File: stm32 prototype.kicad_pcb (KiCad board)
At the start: 4 copper layers, 135 parts, among them J1 USB_B_Mini, J2 Conn_01x06, J3 Conn_01x02, J4 Conn_01x10, Q1 Q_NMOS_GSD, Q2 Q_NMOS_GSD, Q3 Q_NMOS_GSD, Q4 Q_NMOS_GSD, Q5 Q_NMOS_GSD, Q6 Q_NMOS_GSD, Q7 Q_NMOS_GSD, Q8 Q_NMOS_GSD, Q9 Q_NMOS_GSD, U1 FT232RL, U2 W25Q128JV-DTR, U3 STM32F407VGTx, U4 LD1117S33TR, U5 ESP32, U6 IS25LP016D-JNLE-TR, U7 TPS62203DBVR, Y1 Crystal_GND24, Y2 Crystal_GND24, Y3 Crystal_GND23

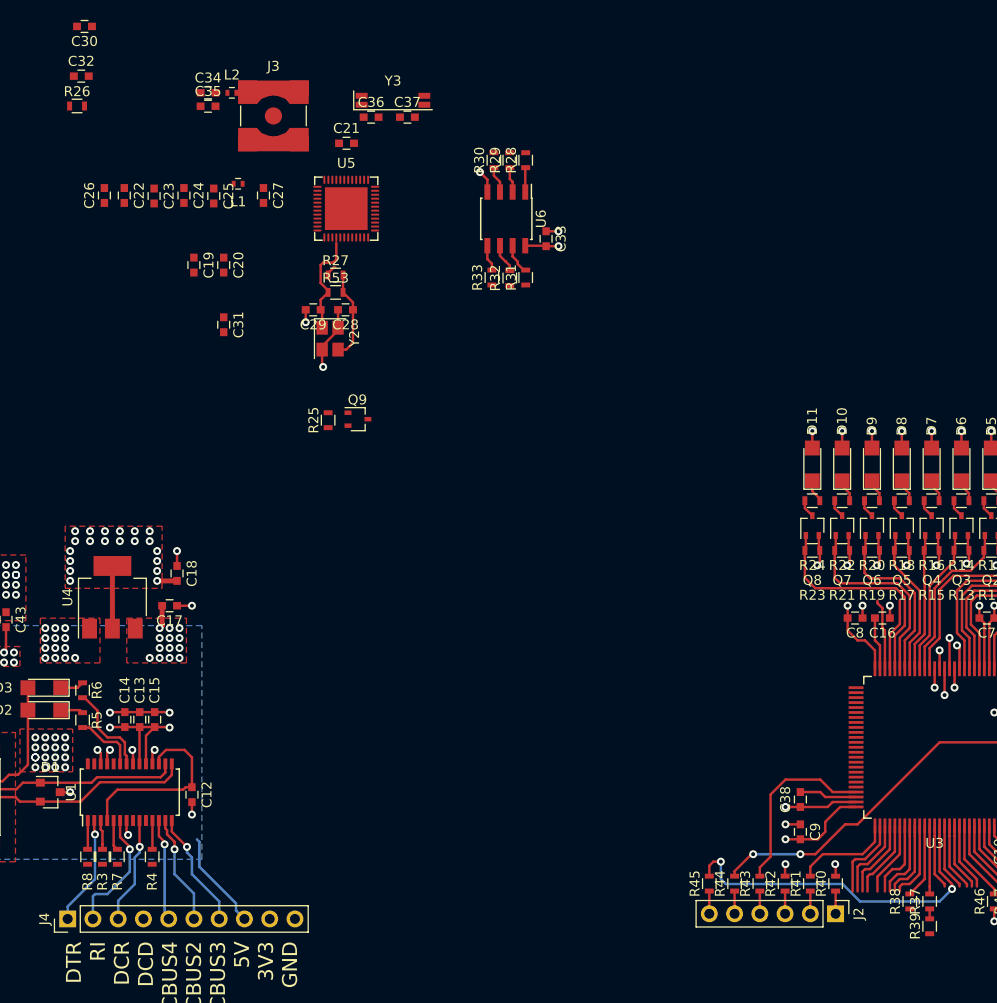
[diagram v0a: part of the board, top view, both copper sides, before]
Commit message: began switching to esp32-wroom module
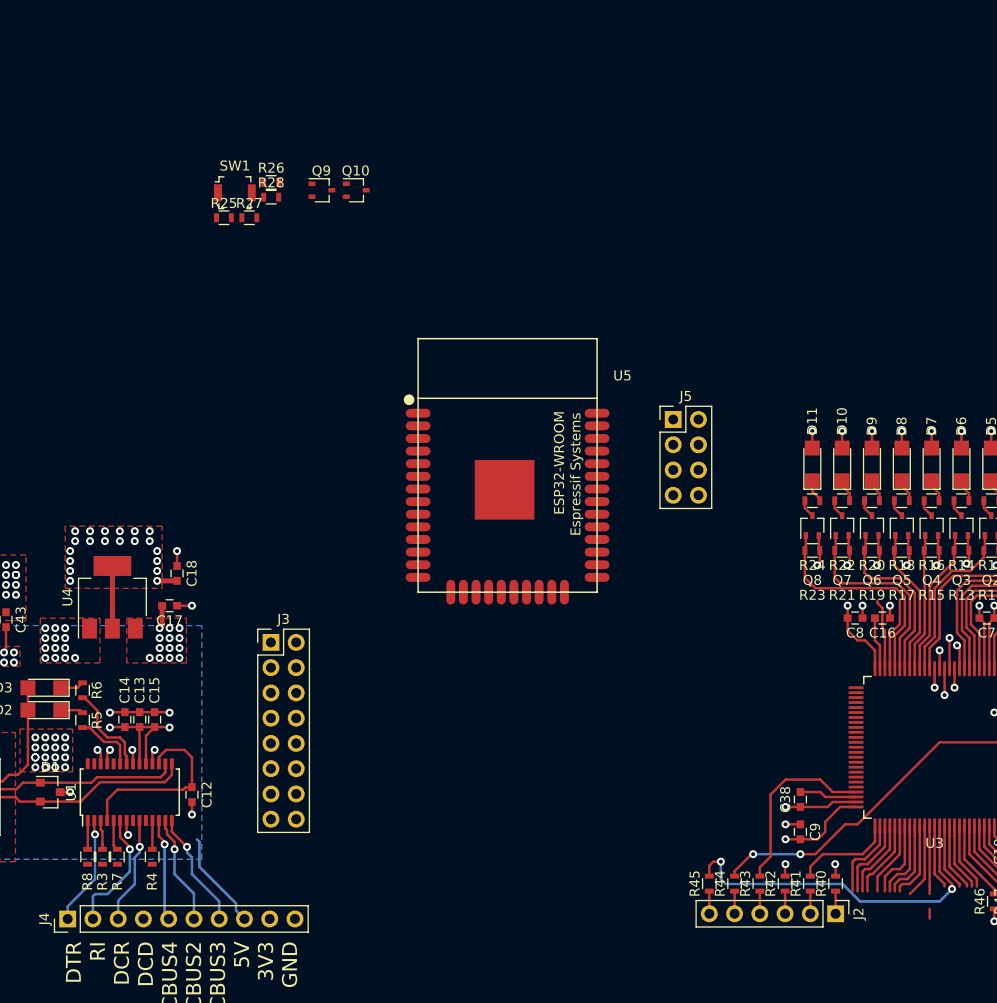
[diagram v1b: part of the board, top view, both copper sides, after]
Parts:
- removed C19, C20, C21, C25, C26, C28, C29, C31, C33, C36, C37: 0.1uF, Capacitors_SMD:C_0603
- removed C22: 10uF, Capacitors_SMD:C_0603
- removed C23, C27: NC, Capacitors_SMD:C_0603
- removed C24: 1uF, Capacitors_SMD:C_0603
- removed C30: 10nF, Capacitors_SMD:C_0603
- removed C32: 3.3nF, Capacitors_SMD:C_0603
- removed C34, C35: C, Capacitors_SMD:C_0603
- removed L1: 2.0nH, Inductors_SMD:L_0402
- removed L2: L, Inductors_SMD:L_0402
- removed R29, R30, R31, R32, R33, R38, R39: 0R, Resistors_SMD:R_0603
- removed R37: 499R, Resistors_SMD:R_0603
- removed R53: 1MR, Resistors_SMD:R_0603
- removed U6: IS25LP016D-JNLE-TR, Housings_SOIC:SOIC-8_3.9x4.9mm_Pitch1.27mm
- removed Y2: Crystal_GND24, Crystals:Crystal_SMD_SeikoEpson_TSX3225-4pin_3.2x2.5mm
- removed Y3: Crystal_GND23, Crystals:Crystal_SMD_SeikoEpson_MC146-4pin_6.7x1.5mm
- added J5: Conn_02x04_Top_Bottom, Pin_Headers:Pin_Header_Straight_2x04_Pitch2.54mm, F.Cu at (150.5, 88.8)
- added Q10: 2N2219, TO_SOT_Packages_SMD:SOT-323_SC-70, F.Cu at (118.6, 65.7)
- added SW1: SW_Push, digikey-footprints:Switch_Tactile_SMD_B3U-1000P, F.Cu at (106.4, 66.0)
- J3: value Conn_01x02 -> Conn_02x08_Top_Bottom; footprint connectors_mdg:SMA_SMD_Jack_Straight -> Pin_Headers:Pin_Header_Straight_2x08_Pitch2.54mm
- Q9: value Q_NMOS_GSD -> 2N2219
- R25: value 10K -> 12k
- R26: value 20k -> 12k
- R27: value 0R -> 12k
- R28: value 0R -> 470R
- U5: value ESP32 -> ESP32-WROOM; footprint ESP32-footprints-Lib:ESP32 -> ESP32-footprints-Lib:ESP32-WROOM
- moved J3 53.0 mm to (110.0, 111.2)
- moved U5 30.5 mm to (133.8, 93.4), turned to 180 degrees
- moved R28 25.9 mm to (110.0, 66.4), turned to 0 degrees
- moved Q9 23.3 mm to (115.1, 65.7)
- moved R25 22.9 mm to (105.3, 68.5), turned to 0 degrees
- moved R26 21.0 mm to (110.0, 64.9)
- moved R27 10.4 mm to (107.8, 68.5)
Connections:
- J3 pad 1: Net-(C35-Pad2) -> Net-(J3-Pad1)
- J3 pad 2: GND -> Net-(J3-Pad1)
- J4 pad 1: FTDI_DTR -> (no net)
- Q9 pad 1: /ESP32_POWER_ENABLE -> FTDI_ES_RTS
- Q9 pad 2: /ESP32_VOLTAGE_SENSE -> Net-(Q9-Pad2)
- Q9 pad 3: +3V3 -> ESP_EN
- R25 pad 1: /ESP32_POWER_ENABLE -> FTDI_ES_DTR
- R25 pad 2: GND -> Net-(Q9-Pad2)
- R26 pad 1: Net-(C32-Pad1) -> FTDI_ES_RTS
- R26 pad 2: Net-(C30-Pad1) -> Net-(Q10-Pad2)
- R27 pad 1: Net-(R27-Pad1) -> +3V3
- R27 pad 2: Net-(C28-Pad1) -> ESP_EN
- R28 pad 1: Net-(R28-Pad1) -> ESP_EN
- R28 pad 2: SD_CMD -> Net-(R28-Pad2)
- R3 pad 1: FTDI_RTS -> Net-(J3-Pad5)
- R7 pad 1: FTDI_RXD -> FTDI_ST_RXD
- R8 pad 1: FTDI_TXD -> FTDI_ST_TXD
- U1 pad 1: FTDI_TXD -> Net-(J3-Pad1)
- U1 pad 2: FTDI_DTR -> Net-(J3-Pad7)
- U1 pad 5: FTDI_RXD -> Net-(J3-Pad3)
- U3 pad 15: /ESP32_VOLTAGE_SENSE -> (no net)
- U3 pad 53: /ESP32_POWER_ENABLE -> (no net)
- U3 pad 54: /ESP32_CHIP_ENABLE -> (no net)
- U3 pad 70: FTDI_RTS -> FTDI_ST_RTS
- U3 pad 86: ESP32_RXD -> ST_ESP_RXD
- U3 pad 87: ESP32_TXD -> ST_ESP_TXD
- U5 pad 1: /ESP32_VOLTAGE_SENSE -> GND
- U5 pad 12: Net-(C36-Pad1) -> (no net)
- U5 pad 13: Net-(C37-Pad1) -> (no net)
- U5 pad 15: (no net) -> GND
- U5 pad 19: /ESP32_VOLTAGE_SENSE -> (no net)
- U5 pad 2: Net-(C34-Pad2) -> +3V3
- U5 pad 25: (no net) -> ESP_GPIO_0
- U5 pad 26: /ESP32_VOLTAGE_SENSE -> (no net)
- U5 pad 28: SD_DATA_2 -> (no net)
- U5 pad 29: SD_DATA_3 -> (no net)
- U5 pad 3: Net-(C27-Pad1) -> ESP_EN
- U5 pad 30: SD_CMD -> (no net)
- U5 pad 31: SD_CLK -> (no net)
- U5 pad 32: SD_DATA_0 -> (no net)
- U5 pad 33: SD_DATA_1 -> (no net)
- U5 pad 34: (no net) -> Net-(J5-Pad3)
- U5 pad 35: (no net) -> Net-(J5-Pad1)
- U5 pad 37: /ESP32_VOLTAGE_SENSE -> (no net)
- U5 pad 38: (no net) -> GND
- U5 pad 39: (no net) -> GND
- U5 pad 4: Net-(C27-Pad1) -> (no net)
- U5 pad 9: /ESP32_CHIP_ENABLE -> (no net)
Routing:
- net (no net): track 235.6 -> 251.7 mm
- net /ESP32_VOLTAGE_SENSE: track 13.0 -> 0.00 mm
- net GND: track 121.2 -> 110.0 mm, vias 77 -> 73
- net Net-(J3-Pad7): track 0.00 -> 11.1 mm, vias 0 -> 1
- net FTDI_DTR: track 11.1 -> 0.00 mm, vias 1 -> 0
- net Net-(C29-Pad1): track 10.5 -> 0.00 mm
- net Net-(C28-Pad1): track 9.02 -> 0.00 mm
- net ST_ESP_RXD: track 0.00 -> 7.47 mm
- net ESP32_RXD: track 7.47 -> 0.00 mm
- net ST_ESP_TXD: track 0.00 -> 6.85 mm
- net ESP32_TXD: track 6.85 -> 0.00 mm
- net +3V3: track 119.3 -> 116.0 mm, vias 53 -> 52
- net Net-(R31-Pad2): track 3.11 -> 0.00 mm
- net FTDI_RXD: track 3.06 -> 0.00 mm
- net Net-(R32-Pad2): track 2.91 -> 0.00 mm
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
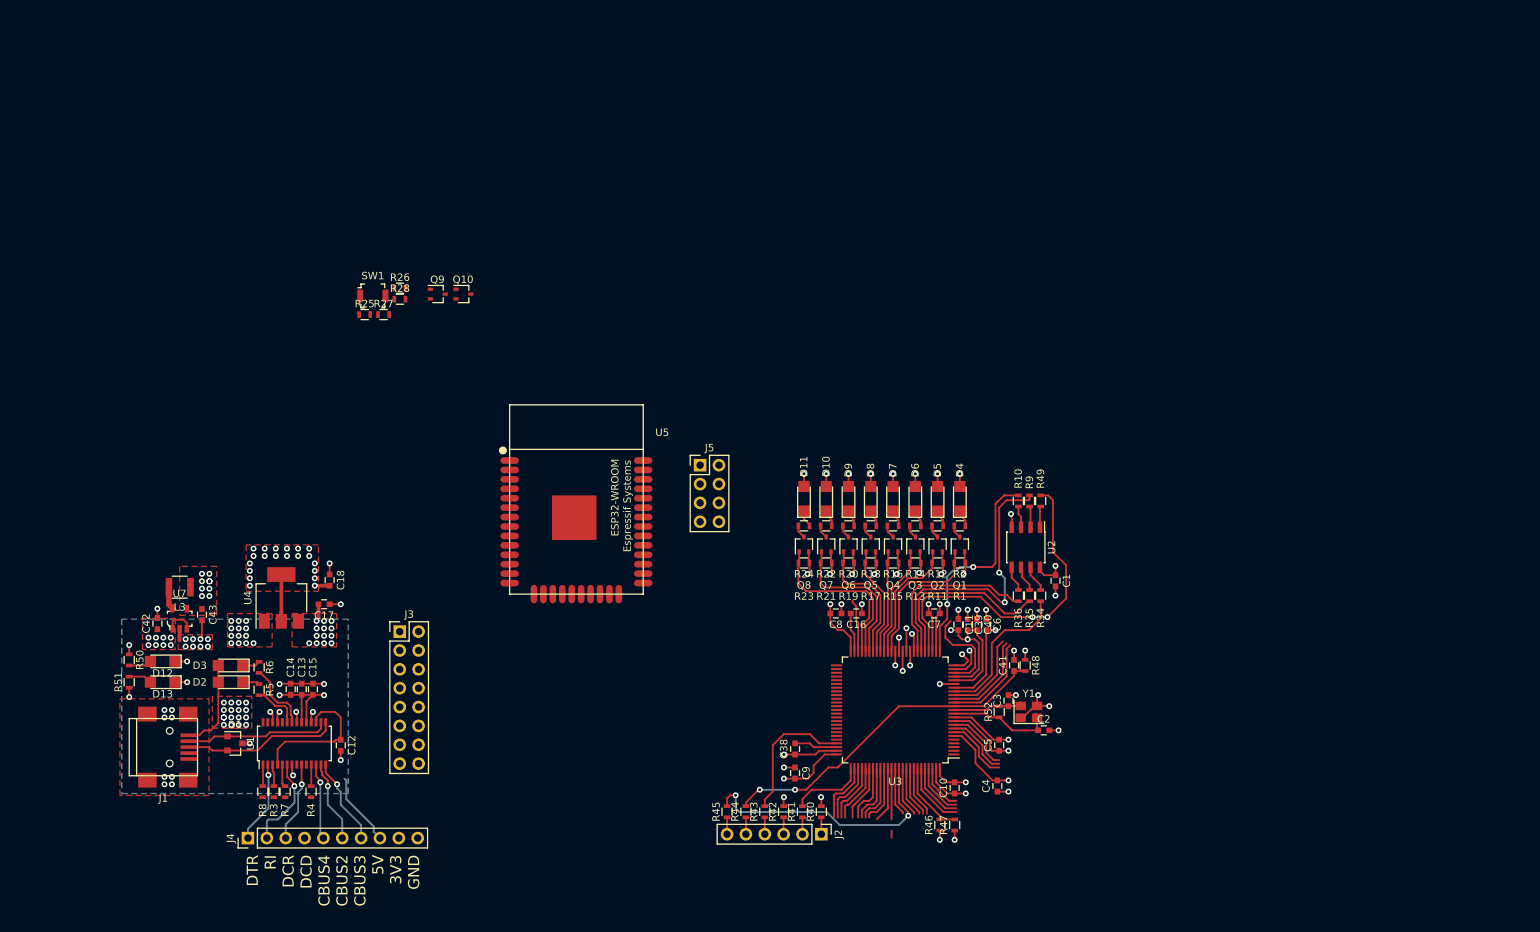
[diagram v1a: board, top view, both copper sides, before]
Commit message: added push button to stm32, worked on some layout
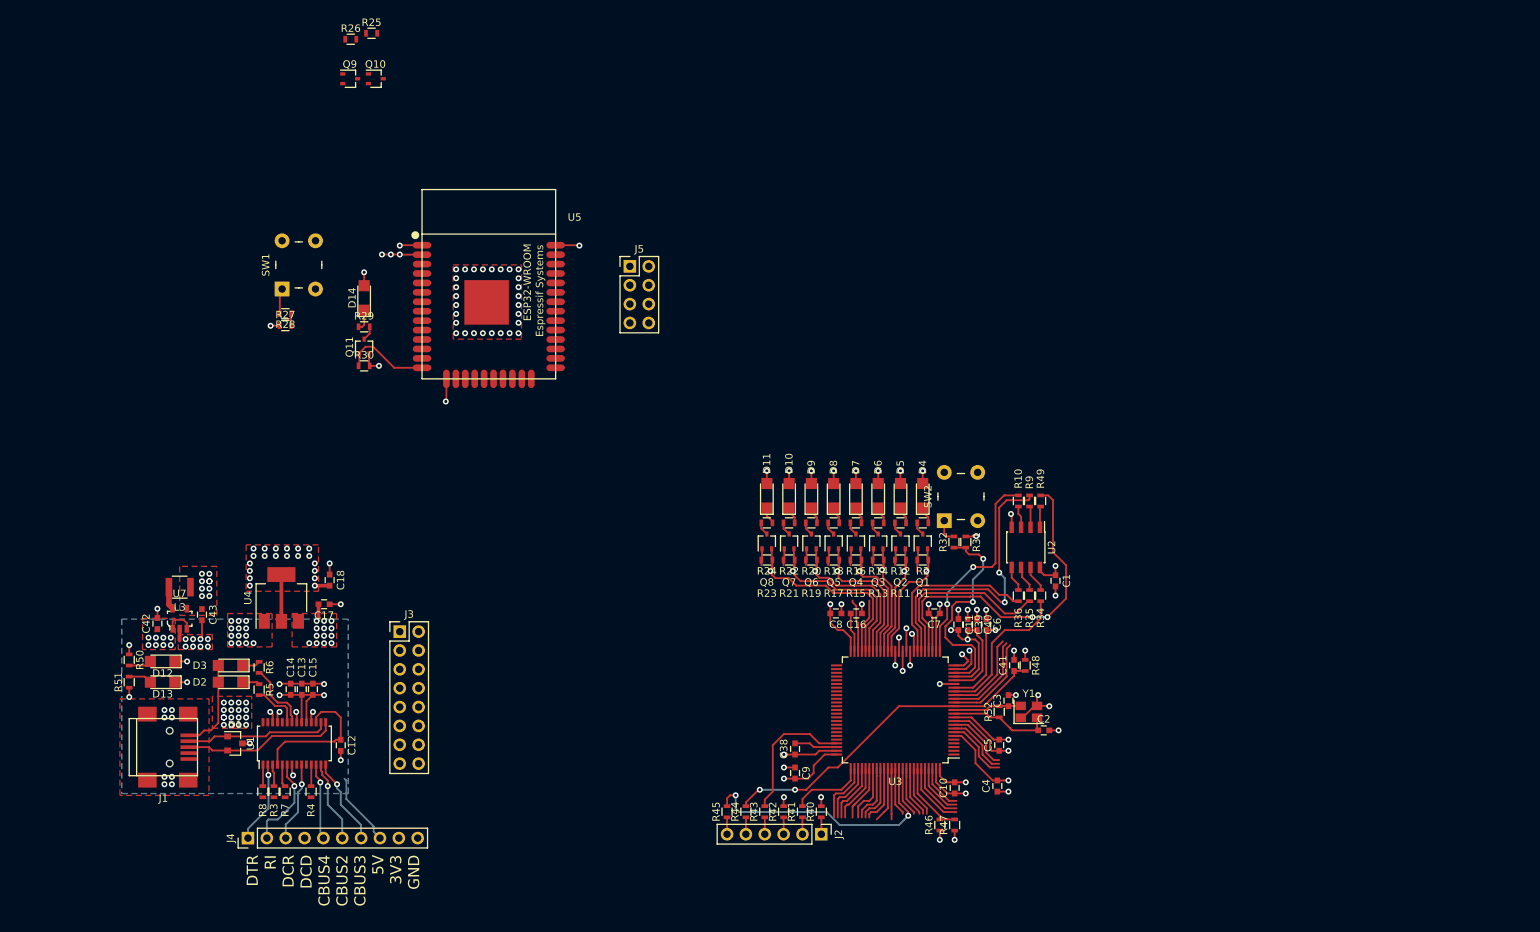
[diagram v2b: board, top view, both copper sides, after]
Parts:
- added D14: LED, LEDs:LED_1206, F.Cu at (105.2, 66.2)
- added Q11: Q_NMOS_GSD, TO_SOT_Packages_SMD:SOT-323_SC-70, F.Cu at (105.2, 72.8)
- added R29: 330R, Resistors_SMD:R_0603, F.Cu at (105.2, 70.1)
- added R30: 10K, Resistors_SMD:R_0603, F.Cu at (105.2, 75.4)
- added R31: 12k, Resistors_SMD:R_0603, F.Cu at (186.3, 99.1)
- added R32: 470R, Resistors_SMD:R_0603, F.Cu at (184.7, 99.1)
- added SW2: SW_Push, switches_mdg:Switch_Tactile_6x6mm_Vertical_SMD_MJTP1230, F.Cu at (185.6, 93.0)
- SW1: footprint digikey-footprints:Switch_Tactile_SMD_B3U-1000P -> switches_mdg:Switch_Tactile_6x6mm_Vertical_SMD_MJTP1230
- moved R25 37.9 mm to (106.2, 30.6)
- moved R26 34.2 mm to (103.4, 31.4)
- moved Q10 31.3 mm to (106.8, 36.7)
- moved Q9 31.3 mm to (103.3, 36.7)
- moved U5 31.3 mm to (122.0, 64.4)
- moved J5 28.4 mm to (141.0, 62.0)
- moved R28 15.6 mm to (94.6, 68.4), turned to 180 degrees
- moved R27 13.3 mm to (94.6, 70.0)
- moved SW1 10.8 mm to (96.4, 61.8), turned to 90 degrees
- moved Q1 5.02 mm to (180.4, 99.0)
- moved Q2 5.02 mm to (177.4, 99.0)
- moved Q3 5.02 mm to (174.4, 99.0)
- moved Q4 5.02 mm to (171.4, 99.0)
- moved Q5 5.02 mm to (168.4, 99.0)
- moved Q6 5.02 mm to (165.4, 99.0)
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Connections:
- J4 pad 1: (no net) -> Net-(J3-Pad7)
- SW1 pad 2: GND -> (no net)
- U3 pad 23: (no net) -> Net-(R31-Pad2)
- U5 pad 14: (no net) -> Net-(Q11-Pad1)
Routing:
- net Net-(R31-Pad2): track 0.00 -> 29.8 mm, vias 0 -> 2
- net (no net): track 251.7 -> 238.2 mm
- net GND: track 110.0 -> 122.2 mm, vias 73 -> 105
- net Net-(Q11-Pad1): track 0.00 -> 11.7 mm
- net +3V3: track 116.0 -> 125.8 mm, vias 52 -> 58
- net STATUS_BIT4: track 14.9 -> 19.4 mm
- net STATUS_BIT5: track 17.7 -> 21.4 mm
- net Net-(R28-Pad2): track 0.00 -> 3.46 mm
- net Net-(R32-Pad2): track 0.00 -> 3.28 mm
- net STATUS_BIT6: track 20.4 -> 23.6 mm
- net STATUS_BIT7: track 22.8 -> 26.0 mm
- net STATUS_BIT3: track 13.9 -> 17.1 mm
- net STATUS_BIT0: track 19.9 -> 16.8 mm
- net Net-(D14-Pad1): track 0.00 -> 2.84 mm
- net Net-(Q11-Pad3): track 0.00 -> 1.97 mm
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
